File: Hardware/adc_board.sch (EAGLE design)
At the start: 21 parts, among them U1 ADS1015, U2 PCA9306

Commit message: Board ready for review
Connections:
- removed net LV_SCL: R4.1, U2.SCL1
- removed net LV_SDA: R5.1, U2.SDA1
- removed net SCL: SJ4.2
- removed net SDA: SJ3.2
- removed net VDD: C1.1, C2.1, R1.2, R2.2, R3.2, SJ2.2, U1.VDD
- net ADDR: now also U1.ADDR; no longer U1.ALERT/RDY
- net GP19_I2C_1_SCL: now also R4.1, U2.SCL1
- net GP20_I2C_1_SDA: now also R5.1, U2.SDA1
- net HV_SCL: now also SJ4.2
- net HV_SDA: now also SJ3.2
- net VSYS: now also C1.1, C2.1, R1.2, R2.2, R3.2, SJ2.2, U1.VDD
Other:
- note added: "Device address 1001000 (0x72) 1001001 (0x73) 1001010 (0x74) 1001011 (0x75)"
- note added: "I2C Address can be set by jumpers. **One and only one jumper should be closed.** Jumper closed SJ1 (Default) SJ2 SJ3 SJ4"
- moved on the sheet: SJ1, SJ2, SJ3, SJ4

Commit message: Add version info
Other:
- note added: "01"
- note added: "M Hord"
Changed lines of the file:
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@@
 1001010 (0x74)
 1001011 (0x75)</text>
+<text x="237.744" y="6.604" size="3.81" layer="91">01</text>
+<text x="165.1" y="7.62" size="3.81" layer="91">M Hord</text>
 </plain>
 <instances>

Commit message: Updated to new edison.lbr
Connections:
- net N$2 renamed A1-/AIN3
- net N$3 renamed A1+/AIN2
- net N$4 renamed A0-/AIN1
- net N$5 renamed A0+/AIN0
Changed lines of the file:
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@@
 </segment>
 </net>
-<net name="N$2" class="0">
+<net name="A1-/AIN3" class="0">
 <segment>
 <pinref part="JP1" gate="G$1" pin="1"/>
@@
 </segment>
 </net>
-<net name="N$3" class="0">
+<net name="A1+/AIN2" class="0">
 <segment>
 <pinref part="U1" gate="G$1" pin="AIN2"/>
@@
 </segment>
 </net>
-<net name="N$4" class="0">
+<net name="A0-/AIN1" class="0">
 <segment>
 <pinref part="JP1" gate="G$1" pin="5"/>
@@
 </segment>
 </net>
-<net name="N$5" class="0">
+<net name="A0+/AIN0" class="0">
 <segment>
 <pinref part="U1" gate="G$1" pin="AIN0"/>

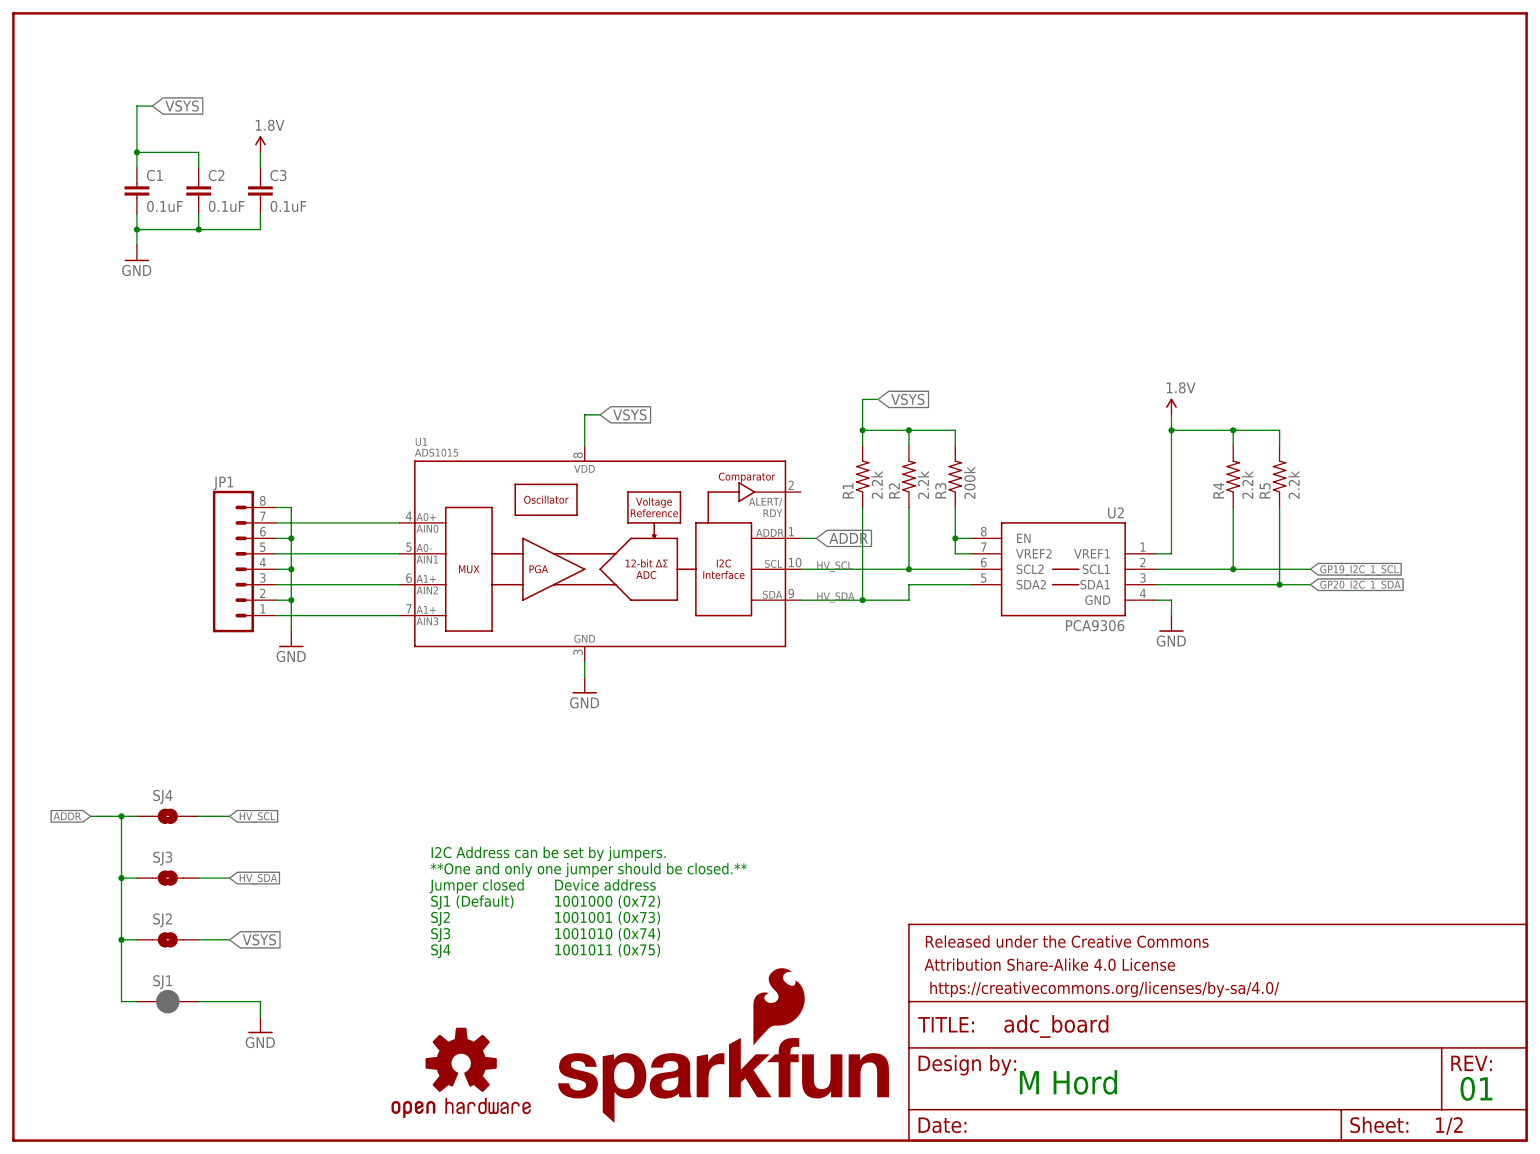
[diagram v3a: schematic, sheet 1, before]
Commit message: Incorporate review feedback
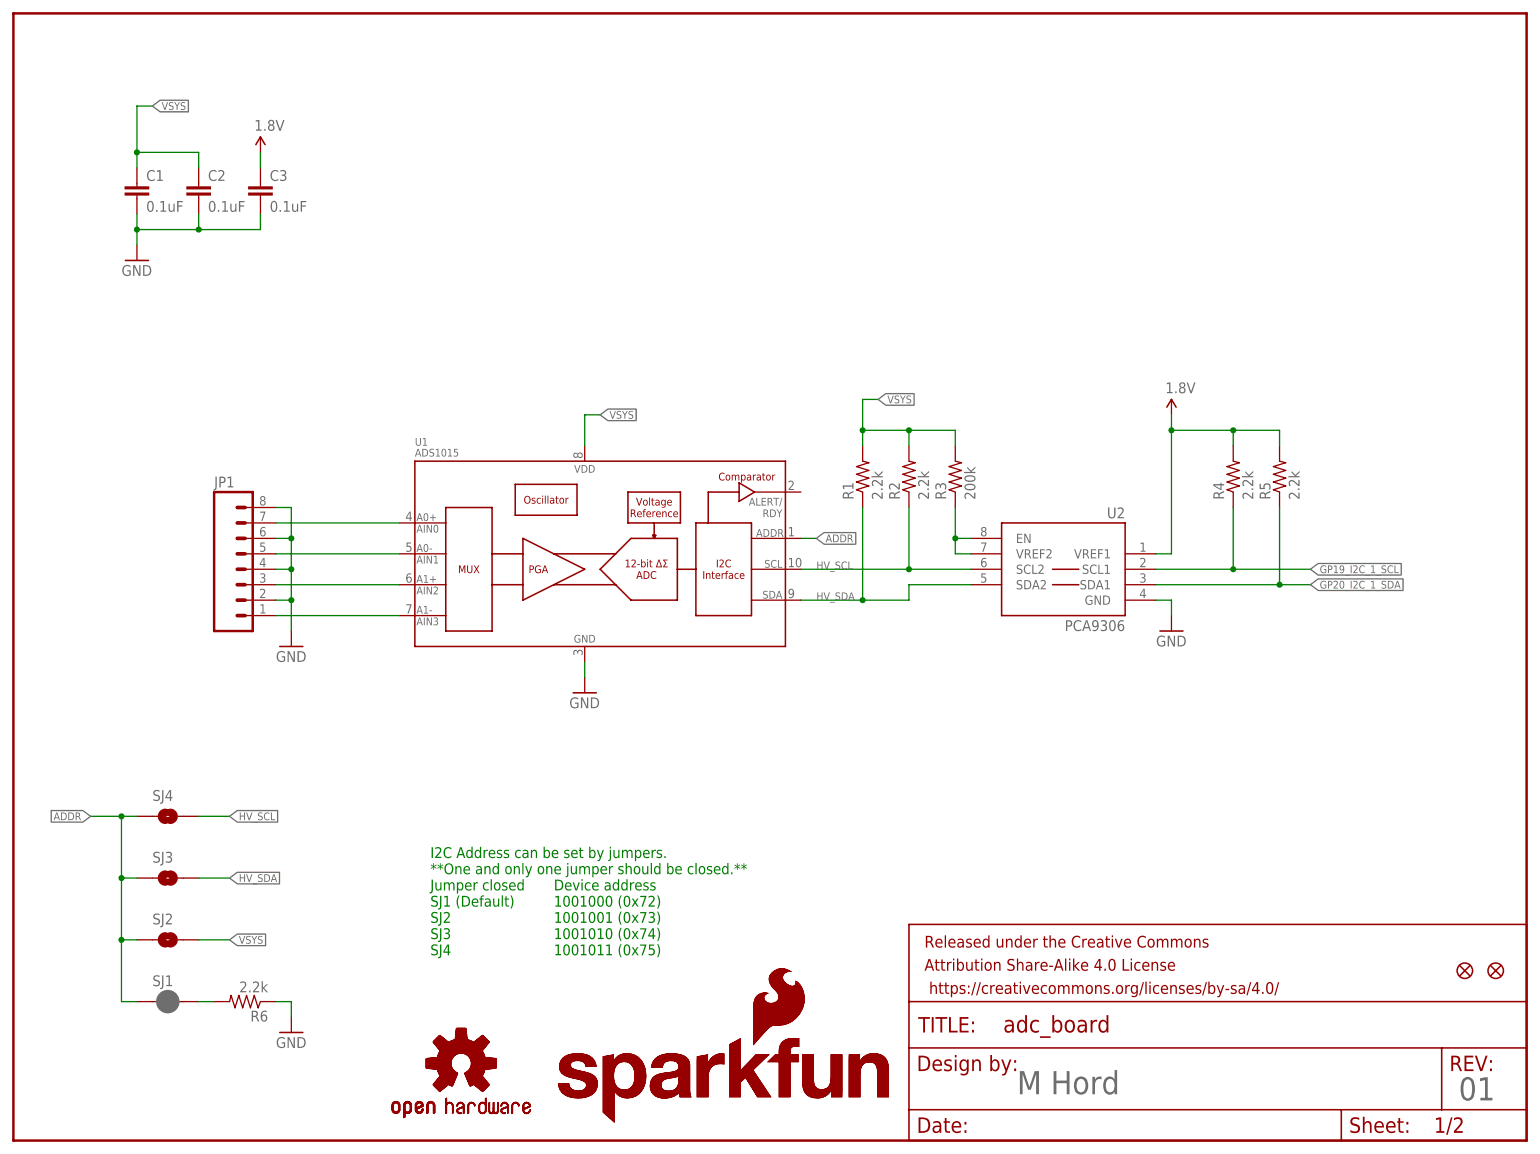
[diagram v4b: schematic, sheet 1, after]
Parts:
- added FID1, FID2: FIDUCIALUFIDUCIAL, SparkFun-Aesthetics:FIDUCIALUFIDUCIAL
- added LOGO1: SFE_LOGO_NAME_FLAME.1_INCH, SparkFun-Aesthetics:SFE_LOGO_NAME_FLAME.1_INCH
- added LOGO4: OSHW-LOGOS, SparkFun-Aesthetics:OSHW-LOGOS
- added R6: 2.2k, SparkFun-Resistors:2.2KOHM1/10W1%(0603)
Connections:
- new net N$3: R6.2, SJ1.2
- net GND: now also R6.1; no longer SJ1.2
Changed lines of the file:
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@@
 <part name="JP1" library="SparkFun-Connectors" deviceset="M08" device="1X08"/>
 <part name="GND7" library="SparkFun-Aesthetics" deviceset="GND" device=""/>
+<part name="LOGO1" library="SparkFun-Aesthetics" deviceset="SFE_LOGO_NAME_FLAME" device=".1_INCH"/>
+<part name="LOGO4" library="SparkFun-Aesthetics" deviceset="OSHW-LOGO" device="S"/>
+<part name="R6" library="SparkFun-Resistors" deviceset="2.2KOHM1/10W1%(0603)" device="" value="2.2k"/>
+<part name="FID1" library="SparkFun-Aesthetics" deviceset="FIDUCIAL" device="UFIDUCIAL"/>
+<part name="FID2" library="SparkFun-Aesthetics" deviceset="FIDUCIAL" device="UFIDUCIAL"/>
 </parts>
 <sheets>
@@
 1001010 (0x74)
 1001011 (0x75)</text>
-<text x="237.744" y="6.604" size="3.81" layer="91">01</text>
-<text x="165.1" y="7.62" size="3.81" layer="91">M Hord</text>
+<text x="237.744" y="6.604" size="3.81" layer="95">01</text>
+<text x="165.1" y="7.62" size="3.81" layer="95">M Hord</text>
 </plain>
 <instances>
@@
 <instance part="GND2" gate="1" x="93.98" y="73.66"/>
 <instance part="GND5" gate="1" x="190.5" y="83.82"/>
-<instance part="GND6" gate="1" x="40.64" y="17.78"/>
+<instance part="GND6" gate="1" x="45.72" y="17.78"/>
 <instance part="JP1" gate="G$1" x="38.1" y="93.98"/>
 <instance part="GND7" gate="1" x="45.72" y="81.28"/>
+<instance part="LOGO1" gate="G$1" x="88.9" y="2.54"/>
+<instance part="LOGO4" gate="G$1" x="73.66" y="12.7"/>
+<instance part="R6" gate="G$1" x="38.1" y="22.86" rot="R180"/>
+<instance part="FID1" gate="G$1" x="243.84" y="27.94"/>
+<instance part="FID2" gate="G$1" x="238.76" y="27.94"/>
 </instances>
 <busses>
@@
 </segment>
 <segment>
-<pinref part="SJ1" gate="G$1" pin="2"/>
 <pinref part="GND6" gate="1" pin="GND"/>
-<wire x1="30.48" y1="22.86" x2="40.64" y2="22.86" width="0.1524" layer="91"/>
-<wire x1="40.64" y1="22.86" x2="40.64" y2="20.32" width="0.1524" layer="91"/>
+<wire x1="45.72" y1="22.86" x2="45.72" y2="20.32" width="0.1524" layer="91"/>
+<pinref part="R6" gate="G$1" pin="1"/>
+<wire x1="43.18" y1="22.86" x2="45.72" y2="22.86" width="0.1524" layer="91"/>
 </segment>
 <segment>
@@
 <pinref part="U1" gate="G$1" pin="ADDR"/>
 <wire x1="129.54" y1="99.06" x2="132.08" y2="99.06" width="0.1524" layer="91"/>
-<label x="132.08" y="99.06" size="1.778" layer="95" xref="yes"/>
+<label x="132.08" y="99.06" size="1.27" layer="95" xref="yes"/>
 </segment>
 </net>
@@
 <wire x1="20.32" y1="162.56" x2="20.32" y2="170.18" width="0.1524" layer="91"/>
 <wire x1="20.32" y1="170.18" x2="22.86" y2="170.18" width="0.1524" layer="91"/>
-<label x="22.86" y="170.18" size="1.778" layer="95" xref="yes"/>
+<label x="22.86" y="170.18" size="1.27" layer="95" xref="yes"/>
 </segment>
 <segment>
@@
 <wire x1="93.98" y1="114.3" x2="93.98" y2="119.38" width="0.1524" layer="91"/>
 <wire x1="93.98" y1="119.38" x2="96.52" y2="119.38" width="0.1524" layer="91"/>
-<label x="96.52" y="119.38" size="1.778" layer="91" xref="yes"/>
+<label x="96.52" y="119.38" size="1.27" layer="95" xref="yes"/>
 </segment>
 <segment>
@@
 <wire x1="139.7" y1="116.84" x2="139.7" y2="121.92" width="0.1524" layer="91"/>
 <wire x1="139.7" y1="121.92" x2="142.24" y2="121.92" width="0.1524" layer="91"/>
-<label x="142.24" y="121.92" size="1.778" layer="95" xref="yes"/>
-</segment>
-<segment>
+<label x="142.24" y="121.92" size="1.27" layer="95" xref="yes"/>
+</segment>
+<segment>
+<label x="35.56" y="33.02" size="1.27" layer="95" xref="yes"/>
 <pinref part="SJ2" gate="G$1" pin="2"/>
-<wire x1="30.48" y1="33.02" x2="35.56" y2="33.02" width="0.1524" layer="91"/>
-<label x="35.56" y="33.02" size="1.778" layer="95" xref="yes"/>
-</segment>
-</net>
+<wire x1="35.56" y1="33.02" x2="30.48" y2="33.02" width="0.1524" layer="91"/>
+</segment>
+</net>
+<net name="N$3" class="0">
+<segment>
+<pinref part="SJ1" gate="G$1" pin="2"/>
+<pinref part="R6" gate="G$1" pin="2"/>
+<wire x1="30.48" y1="22.86" x2="33.02" y2="22.86" width="0.1524" layer="91"/>
+</segment>
+</net>

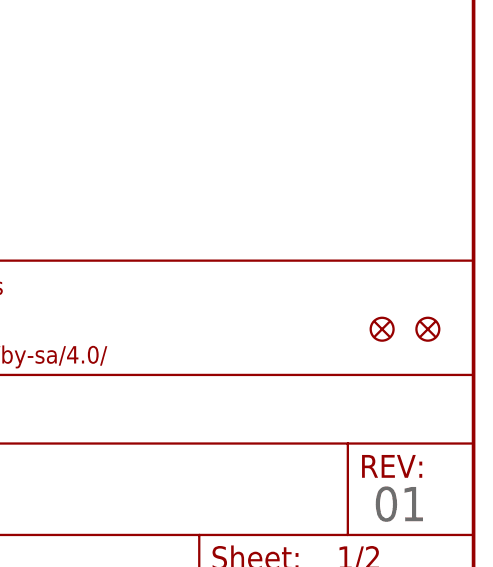
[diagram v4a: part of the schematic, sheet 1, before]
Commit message: Fix fids, remove weird name
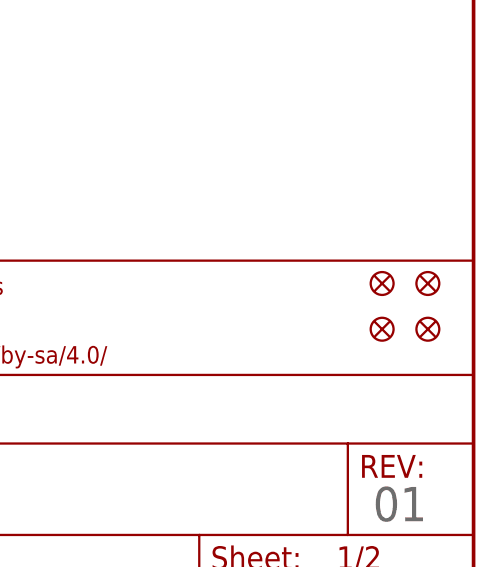
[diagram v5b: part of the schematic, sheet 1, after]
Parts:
- added FID3, FID4: FIDUCIAL1X2, SparkFun-Aesthetics:FIDUCIAL1X2
- FID1, FID2: value FIDUCIALUFIDUCIAL -> FIDUCIAL1X2; device SparkFun-Aesthetics:FIDUCIALUFIDUCIAL -> SparkFun-Aesthetics:FIDUCIAL1X2
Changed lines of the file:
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@@
 <part name="LOGO4" library="SparkFun-Aesthetics" deviceset="OSHW-LOGO" device="S"/>
 <part name="R6" library="SparkFun-Resistors" deviceset="2.2KOHM1/10W1%(0603)" device="" value="2.2k"/>
-<part name="FID1" library="SparkFun-Aesthetics" deviceset="FIDUCIAL" device="UFIDUCIAL"/>
-<part name="FID2" library="SparkFun-Aesthetics" deviceset="FIDUCIAL" device="UFIDUCIAL"/>
+<part name="FID1" library="SparkFun-Aesthetics" deviceset="FIDUCIAL" device="1X2" value="FIDUCIAL1X2"/>
+<part name="FID2" library="SparkFun-Aesthetics" deviceset="FIDUCIAL" device="1X2" value="FIDUCIAL1X2"/>
+<part name="FID3" library="SparkFun-Aesthetics" deviceset="FIDUCIAL" device="1X2" value="FIDUCIAL1X2"/>
+<part name="FID4" library="SparkFun-Aesthetics" deviceset="FIDUCIAL" device="1X2" value="FIDUCIAL1X2"/>
 </parts>
 <sheets>
@@
 <instance part="FID1" gate="G$1" x="243.84" y="27.94"/>
 <instance part="FID2" gate="G$1" x="238.76" y="27.94"/>
+<instance part="FID3" gate="G$1" x="238.76" y="33.02"/>
+<instance part="FID4" gate="G$1" x="243.84" y="33.02"/>
 </instances>
 <busses>
